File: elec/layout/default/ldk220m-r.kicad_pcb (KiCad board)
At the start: 2 copper layers, 5 parts

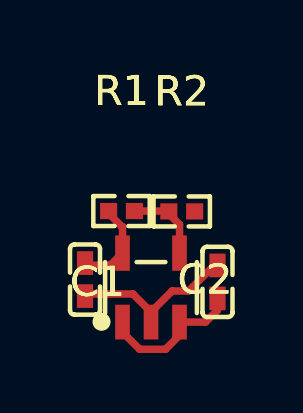
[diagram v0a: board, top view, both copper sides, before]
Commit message: Update to 0.3 syntax, use regulator defintion from library
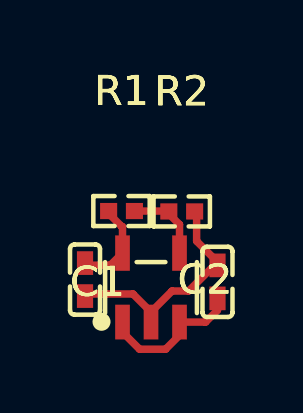
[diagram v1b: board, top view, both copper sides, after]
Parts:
- R1: value 1kΩ ±1% 62.5mW -> 18kΩ ±1% 62.5mW
- R2: value 1kΩ ±1% 62.5mW -> 10kΩ ±1% 62.5mW
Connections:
- net hv renamed OUT
- net out renamed ADJ_NC
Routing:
- net gnd: track 5.62 -> 7.73 mm

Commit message: update layout for kicad9, fix default entry for layout reuse to work
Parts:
- R1: value 18kΩ ±1% 62.5mW -> 10kΩ ±1% 62.5mW
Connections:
- net IN renamed EN
